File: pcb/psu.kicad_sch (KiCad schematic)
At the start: 13 parts, among them CN1 WJ15EDGK-3.81-02P-14-00A, P1 WJ15EDGRC-3.81-2P, U11 15uH, U6 LMR38020SDDAR

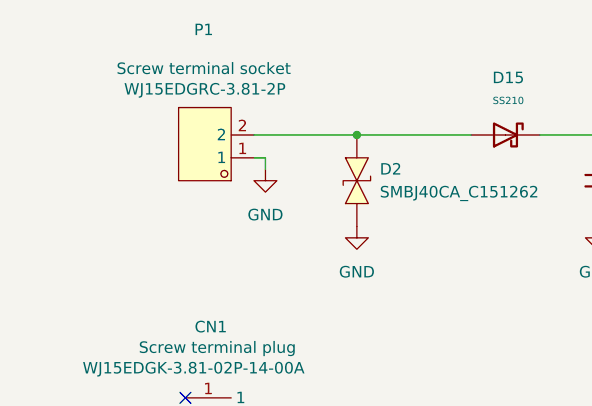
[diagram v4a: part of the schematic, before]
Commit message: sch: add 1A fuse
Adds a 1A fuse before the TVS diodes. Helps protect against shorted input caps or large overvoltage surge. Fixes #44
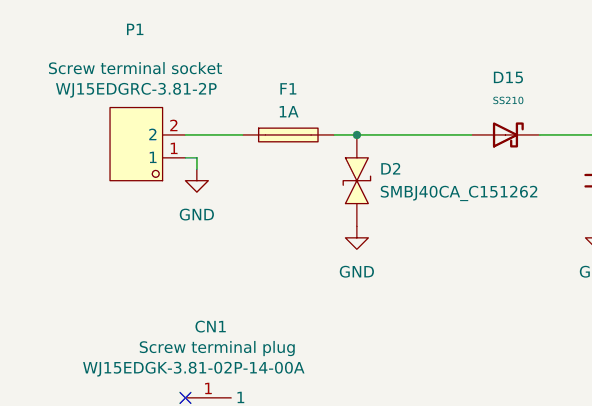
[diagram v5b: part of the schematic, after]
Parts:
- added F1: 1A, EasyEDA:FUSE-SMD_L6.1-W2.6, symbol EasyEDA:0451001.MRL
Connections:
- net at D15.2, D2.2 (A): now also F1.2; no longer P1.2
- new net: F1.1, P1.2
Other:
- moved on the sheet: P1
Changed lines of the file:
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@@
+	)
+	(junction
+		(at 58.42 38.1)
+		(diameter 0)
+		(color 0 0 0 0)
 	)
 	(junction
@@
 	)
 	(junction
-		(at 58.42 38.1)
-		(diameter 0)
-		(color 0 0 0 0)
-	)
-	(junction
 		(at 143.51 38.1)
 		(diameter 0)
@@
 	(wire
 		(pts
-			(xy 46.99 40.64) (xy 48.26 40.64)
+			(xy 40.64 40.64) (xy 39.37 40.64)
 		)
 		(stroke
@@
 	(wire
 		(pts
+			(xy 39.37 38.1) (xy 45.72 38.1)
+		)
+		(stroke
+			(width 0)
+			(type default)
+		)
+	)
+	(wire
+		(pts
 			(xy 85.09 46.99) (xy 85.09 48.26)
 		)
@@
 	(wire
 		(pts
-			(xy 46.99 38.1) (xy 58.42 38.1)
+			(xy 55.88 38.1) (xy 58.42 38.1)
 		)
 		(stroke
@@
 	(wire
 		(pts
-			(xy 48.26 40.64) (xy 48.26 41.91)
+			(xy 40.64 40.64) (xy 40.64 41.91)
 		)
 		(stroke
@@
 	)
 	(symbol
+		(lib_id "EasyEDA:0451001.MRL")
+		(at 50.8 38.1 0)
+		(unit 1)
+		(body_style 1)
+		(exclude_from_sim no)
+		(in_bom yes)
+		(on_board yes)
+		(in_pos_files yes)
+		(dnp no)
+		(fields_autoplaced yes)
+		(property "Reference" "F1"
+			(at 50.8 33.02 0)
+			(show_name no)
+			(do_not_autoplace no)
+			(effects
+				(font
+					(size 1.27 1.27)
+				)
+			)
+		)
+		(property "Value" "1A"
+			(at 50.8 35.56 0)
+			(show_name no)
+			(do_not_autoplace no)
+			(effects
+				(font
+					(size 1.27 1.27)
+				)
+			)
+		)
+		(property "Footprint" "EasyEDA:FUSE-SMD_L6.1-W2.6"
+			(at 50.8 45.72 0)
+			(hide yes)
+			(show_name no)
+			(do_not_autoplace no)
+			(effects
+				(font
+					(size 1.27 1.27)
+				)
+			)
+		)
+		(property "Datasheet" "https://lcsc.com/product-detail/Surface-Mount-Fuses_Littelfuse_0451001-MRL_1A-125V_C3099.html"
+			(at 50.8 48.26 0)
+			(hide yes)
+			(show_name no)
+			(do_not_autoplace no)
+			(effects
+				(font
+					(size 1.27 1.27)
+				)
+			)
+		)
+		(property "Description" "1A 125V"
+			(at 50.8 60.96 0)
+			(hide yes)
+			(show_name no)
+			(do_not_autoplace no)
+			(effects
+				(font
+					(size 1.27 1.27)
+				)
+			)
+		)
+		(property "Manufacturer" "Littelfuse(美国力特)"
+			(at 50.8 50.8 0)
+			(hide yes)
+			(show_name no)
+			(do_not_autoplace no)
+			(effects
+				(font
+					(size 1.27 1.27)
+				)
+			)
+		)
+		(property "MPN" "0451001.MRL"
+			(at 50.8 53.34 0)
+			(hide yes)
+			(show_name no)
+			(do_not_autoplace no)
+			(effects
+				(font
+					(size 1.27 1.27)
+				)
+			)
+		)
+		(property "LCSC Part" "C3099"
+			(at 50.8 55.88 0)
+			(hide yes)
+			(show_name no)
+			(do_not_autoplace no)
+			(effects
+				(font
+					(size 1.27 1.27)
+				)
+			)
+		)
+		(pin "1"
+		)
+		(pin "2"
+		)
+		(instances
+			(project "EveningStar"
+				(path "/4c61f5a2-f8d4-462a-9bc3-d74437d30372/2e538fbd-4766-4d3c-804f-b602af6e3385"
+					(reference "F1")
+					(unit 1)
+				)
+			)
+		)
+	)
+	(symbol
 		(lib_id "PCM_JLCPCB-Capacitors:0805,100nF")
 		(at 95.25 43.18 0)
@@
 	(symbol
 		(lib_id "power:GND")
-		(at 48.26 41.91 0)
+		(at 40.64 41.91 0)
 		(unit 1)
 		(body_style 1)
@@
 		(fields_autoplaced yes)
 		(property "Reference" "#PWR032"
-			(at 48.26 48.26 0)
+			(at 40.64 48.26 0)
 			(hide yes)
 			(show_name no)
@@
 		)
 		(property "Value" "GND"
-			(at 48.26 46.99 0)
+			(at 40.64 46.99 0)
 			(show_name no)
 			(do_not_autoplace no)
@@
 		)
 		(property "Footprint" ""
-			(at 48.26 41.91 0)
+			(at 40.64 41.91 0)
 			(hide yes)
 			(show_name no)
@@
 		)
 		(property "Datasheet" ""
-			(at 48.26 41.91 0)
+			(at 40.64 41.91 0)
 			(hide yes)
 			(show_name no)
@@
 		)
 		(property "Description" "Power symbol creates a global label with name \"GND\" , ground"
-			(at 48.26 41.91 0)
+			(at 40.64 41.91 0)
 			(hide yes)
 			(show_name no)
@@
 	(symbol
 		(lib_id "EasyEDA:WJ15EDGRC-3.81-2P")
-		(at 43.18 39.37 180)
+		(at 35.56 39.37 180)
 		(unit 1)
 		(body_style 1)
@@
 		(dnp no)
 		(property "Reference" "P1"
-			(at 41.402 26.416 0)
+			(at 33.782 26.416 0)
 			(show_name no)
 			(do_not_autoplace no)
@@
 		)
 		(property "Value" "WJ15EDGRC-3.81-2P"
-			(at 41.53 33.02 0)
+			(at 33.91 33.02 0)
 			(show_name no)
 			(do_not_autoplace no)
@@
 		)
 		(property "Footprint" "EasyEDA:CONN-TH_2P-P3.81_WJ15EDGRC-3.81-2P"
-			(at 43.18 30.48 0)
+			(at 35.56 30.48 0)
 			(hide yes)
 			(show_name no)
@@
 		)
 		(property "Datasheet" "https://lcsc.com/product-detail/15EDG-Connectors_WJ15EDGRC-3-81-2P_C8387.html"
-			(at 43.18 27.94 0)
+			(at 35.56 27.94 0)
 			(hide yes)
 			(show_name no)
@@
 		)
 		(property "Description" "Screw terminal socket"
-			(at 41.402 30.734 0)
+			(at 33.782 30.734 0)
 			(show_name no)
 			(do_not_autoplace no)
@@
 		)
 		(property "Manufacturer" "KANGNEX(康奈克斯电气)"
-			(at 43.18 25.4 0)
+			(at 35.56 25.4 0)
 			(hide yes)
 			(show_name no)
@@
 		)
 		(property "MPN" "WJ15EDGRC-3.81-02P-14-00A"
-			(at 43.18 22.86 0)
+			(at 35.56 22.86 0)
 			(hide yes)
 			(show_name no)
@@
 		)
 		(property "LCSC Part" "C8387"
-			(at 43.18 20.32 0)
-			(hide yes)
-			(show_name no)
+			(at 35.56 20.32 0)
+			(hide yes)
+			(show_name no)

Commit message: sch: fix a bunch of psu drc errors
There were missing power flags, unspecified pin types and a missing connection between SW and feedback divider on the DC-DC IC
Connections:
- net +3V3: now also R15.1
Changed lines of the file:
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@@
+	)
+	(junction
+		(at 143.51 57.15)
+		(diameter 0)
+		(color 0 0 0 0)
+	)
+	(junction
+		(at 85.09 38.1)
+		(diameter 0)
+		(color 0 0 0 0)
+	)
+	(junction
+		(at 58.42 38.1)
+		(diameter 0)
+		(color 0 0 0 0)
+	)
+	(junction
+		(at 40.64 46.99)
+		(diameter 0)
+		(color 0 0 0 0)
+	)
+	(junction
+		(at 157.48 59.69)
+		(diameter 0)
+		(color 0 0 0 0)
+	)
+	(junction
+		(at 95.25 38.1)
+		(diameter 0)
+		(color 0 0 0 0)
+	)
+	(junction
+		(at 85.09 48.26)
+		(diameter 0)
+		(color 0 0 0 0)
 	)
 	(junction
@@
 	)
 	(junction
-		(at 85.09 38.1)
+		(at 130.81 38.1)
 		(diameter 0)
 		(color 0 0 0 0)
 	)
 	(junction
-		(at 58.42 38.1)
+		(at 100.33 38.1)
 		(diameter 0)
 		(color 0 0 0 0)
 	)
 	(junction
-		(at 95.25 38.1)
-		(diameter 0)
-		(color 0 0 0 0)
-	)
-	(junction
-		(at 157.48 59.69)
-		(diameter 0)
-		(color 0 0 0 0)
-	)
-	(junction
-		(at 143.51 57.15)
-		(diameter 0)
-		(color 0 0 0 0)
-	)
-	(junction
-		(at 85.09 48.26)
-		(diameter 0)
-		(color 0 0 0 0)
-	)
-	(junction
-		(at 130.81 38.1)
+		(at 157.48 38.1)
 		(diameter 0)
 		(color 0 0 0 0)
@@
 	(wire
 		(pts
-			(xy 143.51 38.1) (xy 167.64 38.1)
+			(xy 143.51 38.1) (xy 157.48 38.1)
 		)
 		(stroke
@@
 	(wire
 		(pts
-			(xy 95.25 38.1) (xy 105.41 38.1)
+			(xy 95.25 38.1) (xy 100.33 38.1)
+		)
+		(stroke
+			(width 0)
+			(type default)
+		)
+	)
+	(wire
+		(pts
+			(xy 40.64 46.99) (xy 46.99 46.99)
 		)
 		(stroke
@@
 	(wire
 		(pts
+			(xy 100.33 38.1) (xy 105.41 38.1)
+		)
+		(stroke
+			(width 0)
+			(type default)
+		)
+	)
+	(wire
+		(pts
 			(xy 55.88 38.1) (xy 58.42 38.1)
 		)
@@
 	(wire
 		(pts
+			(xy 157.48 36.83) (xy 157.48 38.1)
+		)
+		(stroke
+			(width 0)
+			(type default)
+		)
+	)
+	(wire
+		(pts
 			(xy 167.64 38.1) (xy 167.64 36.83)
 		)
@@
 	(wire
 		(pts
+			(xy 40.64 46.99) (xy 40.64 48.26)
+		)
+		(stroke
+			(width 0)
+			(type default)
+		)
+	)
+	(wire
+		(pts
 			(xy 130.81 38.1) (xy 130.81 39.37)
 		)
@@
 	(wire
 		(pts
-			(xy 40.64 40.64) (xy 40.64 41.91)
-		)
-		(stroke
-			(width 0)
-			(type default)
-		)
-	)
-	(wire
-		(pts
-			(xy 157.48 36.83) (xy 157.48 52.07)
+			(xy 40.64 40.64) (xy 40.64 46.99)
+		)
+		(stroke
+			(width 0)
+			(type default)
+		)
+	)
+	(wire
+		(pts
+			(xy 157.48 38.1) (xy 157.48 52.07)
+		)
+		(stroke
+			(width 0)
+			(type default)
+		)
+	)
+	(wire
+		(pts
+			(xy 157.48 38.1) (xy 167.64 38.1)
 		)
 		(stroke
@@
 	)
 	(symbol
+		(lib_id "power:PWR_FLAG")
+		(at 46.99 46.99 0)
+		(unit 1)
+		(body_style 1)
+		(exclude_from_sim no)
+		(in_bom yes)
+		(on_board yes)
+		(in_pos_files yes)
+		(dnp no)
+		(fields_autoplaced yes)
+		(property "Reference" "#FLG06"
+			(at 46.99 45.085 0)
+			(hide yes)
+			(show_name no)
+			(do_not_autoplace no)
+			(effects
+				(font
+					(size 1.27 1.27)
+				)
+			)
+		)
+		(property "Value" "PWR_FLAG"
+			(at 46.99 41.91 0)
+			(show_name no)
+			(do_not_autoplace no)
+			(effects
+				(font
+					(size 1.27 1.27)
+				)
+			)
+		)
+		(property "Footprint" ""
+			(at 46.99 46.99 0)
+			(hide yes)
+			(show_name no)
+			(do_not_autoplace no)
+			(effects
+				(font
+					(size 1.27 1.27)
+				)
+			)
+		)
+		(property "Datasheet" ""
+			(at 46.99 46.99 0)
+			(hide yes)
+			(show_name no)
+			(do_not_autoplace no)
+			(effects
+				(font
+					(size 1.27 1.27)
+				)
+			)
+		)
+		(property "Description" "Special symbol for telling ERC where power comes from"
+			(at 46.99 46.99 0)
+			(hide yes)
+			(show_name no)
+			(do_not_autoplace no)
+			(effects
+				(font
+					(size 1.27 1.27)
+				)
+			)
+		)
+		(pin "1"
+		)
+		(instances
+			(project "EveningStar"
+				(path "/4c61f5a2-f8d4-462a-9bc3-d74437d30372/2e538fbd-4766-4d3c-804f-b602af6e3385"
+					(reference "#FLG06")
+					(unit 1)
+				)
+			)
+		)
+	)
+	(symbol
 		(lib_id "EasyEDA:SMBJ40CA_C151262")
 		(at 58.42 43.18 90)
@@
 	(symbol
 		(lib_id "power:GND")
-		(at 40.64 41.91 0)
+		(at 40.64 48.26 0)
 		(unit 1)
 		(body_style 1)
@@
 		(fields_autoplaced yes)
 		(property "Reference" "#PWR032"
+			(at 40.64 54.61 0)
+			(hide yes)
+			(show_name no)
+			(do_not_autoplace no)
+			(effects
+				(font
+					(size 1.27 1.27)
+				)
+			)
+		)
+		(property "Value" "GND"
+			(at 40.64 53.34 0)
+			(show_name no)
+			(do_not_autoplace no)
+			(effects
+				(font
+					(size 1.27 1.27)
+				)
+			)
+		)
+		(property "Footprint" ""
 			(at 40.64 48.26 0)
 			(hide yes)
@@
 			)
 		)
-		(property "Value" "GND"
-			(at 40.64 46.99 0)
-			(show_name no)
-			(do_not_autoplace no)
-			(effects
-				(font
-					(size 1.27 1.27)
-				)
-			)
-		)
-		(property "Footprint" ""
-			(at 40.64 41.91 0)
-			(hide yes)
-			(show_name no)
-			(do_not_autoplace no)
-			(effects
-				(font
-					(size 1.27 1.27)
-				)
-			)
-		)
 		(property "Datasheet" ""
-			(at 40.64 41.91 0)
+			(at 40.64 48.26 0)
 			(hide yes)
 			(show_name no)
@@
 		)
 		(property "Description" "Power symbol creates a global label with name \"GND\" , ground"
-			(at 40.64 41.91 0)
+			(at 40.64 48.26 0)
 			(hide yes)
 			(show_name no)
@@
 		(dnp no)
 		(property "Reference" "P1"
-			(at 33.782 26.416 0)
+			(at 34.036 28.956 0)
 			(show_name no)
 			(do_not_autoplace no)
@@
 					(unit 1)
 				)
+			)
+		)
+	)
+	(symbol
+		(lib_id "power:PWR_FLAG")
+		(at 100.33 38.1 0)
+		(unit 1)
+		(body_style 1)
+		(exclude_from_sim no)
+		(in_bom yes)
+		(on_board yes)
+		(in_pos_files yes)
+		(dnp no)
+		(fields_autoplaced yes)
+		(property "Reference" "#FLG04"
+			(at 100.33 36.195 0)
+			(hide yes)
+			(show_name no)
+			(do_not_autoplace no)
+			(effects
+				(font
+					(size 1.27 1.27)
+				)
+			)
+		)
+		(property "Value" "PWR_FLAG"
+			(at 100.33 33.02 0)
+			(show_name no)
+			(do_not_autoplace no)
+			(effects
+				(font
+					(size 1.27 1.27)
+				)
+			)
+		)
+		(property "Footprint" ""
+			(at 100.33 38.1 0)
+			(hide yes)
+			(show_name no)
+			(do_not_autoplace no)
+			(effects
+				(font
+					(size 1.27 1.27)
+				)
+			)
+		)
+		(property "Datasheet" ""
+			(at 100.33 38.1 0)
+			(hide yes)
+			(show_name no)
+			(do_not_autoplace no)
+			(effects
+				(font
+					(size 1.27 1.27)
+				)
+			)
+		)
+		(property "Description" "Special symbol for telling ERC where power comes from"
+			(at 100.33 38.1 0)
+			(hide yes)
+			(show_name no)
+			(do_not_autoplace no)
+			(effects
+				(font
+					(size 1.27 1.27)
+				)
+			)
+		)
+		(pin "1"
+		)
+		(instances
+			(project "EveningStar"
+				(path "/4c61f5a2-f8d4-462a-9bc3-d74437d30372/2e538fbd-4766-4d3c-804f-b602af6e3385"
+					(reference "#FLG04")
+					(unit 1)
+				)
